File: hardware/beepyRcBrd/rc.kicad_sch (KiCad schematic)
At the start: 16 parts, among them J15 Conn_01x04, J16 Conn_01x03, J17 Conn_01x02, J20 Conn_01x04, Q4 BSS138LT1G, U12 AT7456ELAH_C42388749, X2 H6OEL89CSC-SUGYLC-27M

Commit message: fix: net names
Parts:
- U12: symbol lscs:AT7456ELAH_C42388749 -> beepyRc_symbols:AT7456ELAH_C42388749
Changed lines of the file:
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@@
 	)
 	(symbol
-		(lib_id "lscs:AT7456ELAH_C42388749")
+		(lib_id "beepyRc_symbols:AT7456ELAH_C42388749")
 		(at 68.58 162.56 0)
 		(unit 1)

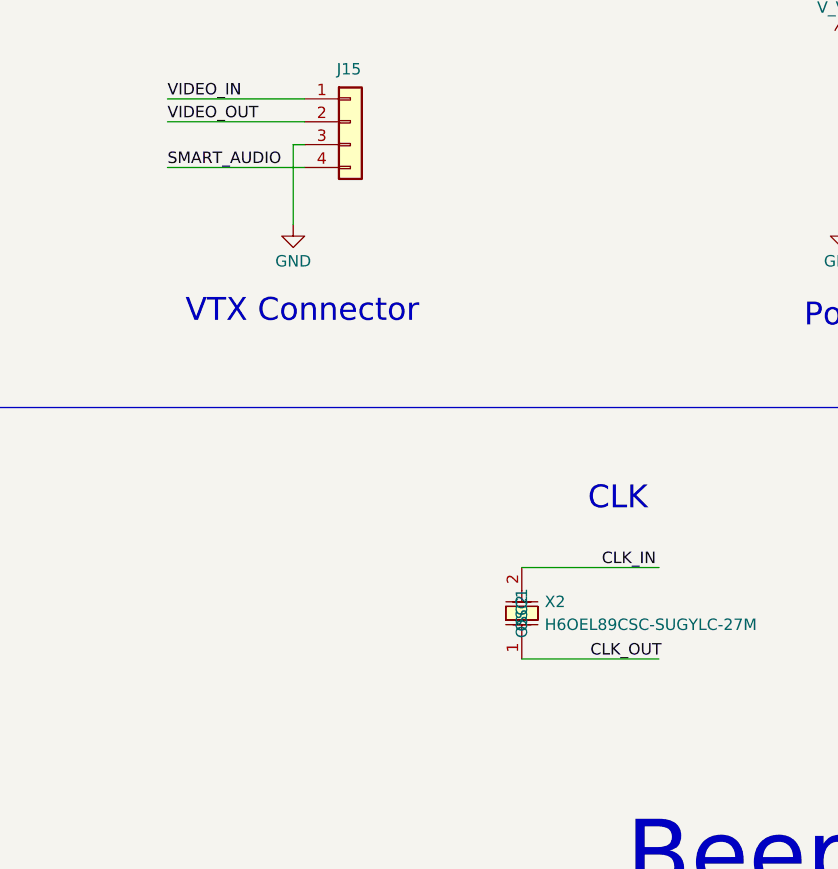
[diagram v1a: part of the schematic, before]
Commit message: fix: passing schematics ERC rules
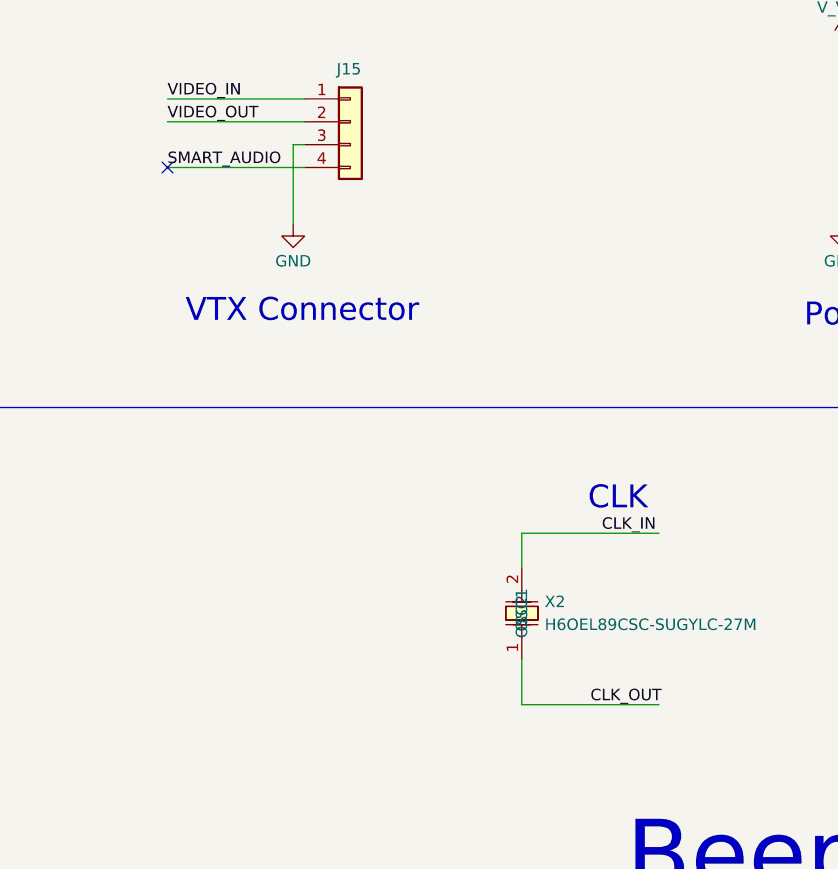
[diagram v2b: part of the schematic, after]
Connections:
- no-connect marks 0 -> 1
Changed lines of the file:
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@@
 		(color 0 0 0 0)
 	)
+	(no_connect
+		(at 158.75 96.52)
+	)
 	(wire
 		(pts
@@
 	(wire
 		(pts
+			(xy 198.12 156.21) (xy 198.12 151.13)
+		)
+		(stroke
+			(width 0)
+			(type default)
+		)
+	)
+	(wire
+		(pts
 			(xy 85.09 152.4) (xy 85.09 167.64)
 		)
@@
 	(wire
 		(pts
+			(xy 198.12 137.16) (xy 198.12 140.97)
+		)
+		(stroke
+			(width 0)
+			(type default)
+		)
+	)
+	(wire
+		(pts
 			(xy 54.61 62.23) (xy 54.61 66.04)
 		)
@@
 	(wire
 		(pts
-			(xy 198.12 151.13) (xy 213.36 151.13)
+			(xy 198.12 156.21) (xy 213.36 156.21)
 		)
 		(stroke
@@
 	(wire
 		(pts
-			(xy 198.12 140.97) (xy 213.36 140.97)
+			(xy 198.12 137.16) (xy 213.36 137.16)
 		)
 		(stroke
@@
 	)
 	(label "CLK_IN"
-		(at 207.01 140.97 0)
+		(at 207.01 137.16 0)
 		(effects
 			(font
@@
 	)
 	(label "CLK_OUT"
-		(at 205.74 151.13 0)
+		(at 205.74 156.21 0)
 		(effects
 			(font

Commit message: feat: completed beepyRcBrd_rev_0_0.pdf
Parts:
- C14, C29, C30, C33, C34, C37: footprint Capacitor_SMD:C_0603_1608Metric_Pad1.08x0.95mm_HandSolder -> beepyRcBrd:C_0603_1608Metric_Pad1.08x0.95mm_HandSolder
- J15, J20: footprint TestPoint:TestPoint_Bridge_Pitch2.54mm_Drill1.0mm -> beepyRcBrd:PinHeader_1x04_P2.54mm_Vertical
- J16: footprint TestPoint:TestPoint_Bridge_Pitch2.54mm_Drill1.0mm -> beepyRcBrd:rc
- J17: footprint TestPoint:TestPoint_Bridge_Pitch2.54mm_Drill1.0mm -> beepyRcBrd:PinHeader_1x02_P2.54mm_Vertical
- Q4: footprint lscs:SOT-23-3_L2.9-W1.6-P1.90-LS2.8-BR -> beepyRcBrd:SOT-23-3_L2.9-W1.6-P1.90-LS2.8-BR
- R20, R33, R34: footprint Resistor_SMD:R_0603_1608Metric_Pad0.98x0.95mm_HandSolder -> beepyRcBrd:R_0603_1608Metric_Pad0.98x0.95mm_HandSolder
- U12: footprint lscs:LGA-16_L6.8-W4.0-P0.65-TL-2EP -> beepyRcBrd:LGA-16_L6.8-W4.0-P0.65-TL-2EP
- X2: footprint lscs:HC-49S_L11.4-W4.8-LS12.7 -> beepyRcBrd:HC-49S_L11.4-W4.8-LS12.7
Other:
- note added: "C33 between AVDD (P12) and AGND (P10) C34 between DVDD (P2) and DGND (P1) C37 between PVDD (P14) and PGND (P11)"
- note removed: "C14 between AVDD (P12) and AGND (P10) C29 between DVDD (P2) and DGND (P1) C30 between PVDD (P14) and PGND (P11)"
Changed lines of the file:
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@@
 		(rev "V0.0")
 		(company "ElectronPlant")
+		(comment 1 "© David Arnaiz 2026")
+		(comment 2 "Licensed under CERN-OHL-S v2")
 	)
 	(text "BeepyRC"
 		(exclude_from_sim no)
-		(at 233.426 173.228 0)
+		(at 252.73 173.99 0)
 		(effects
 			(font
@@
 		)
 	)
-	(text "C14 between AVDD (P12) and AGND (P10)\nC29 between DVDD (P2) and DGND (P1)\nC30 between PVDD (P14) and PGND (P11)"
+	(text "C33 between AVDD (P12) and AGND (P10)\nC34 between DVDD (P2) and DGND (P1)\nC37 between PVDD (P14) and PGND (P11)"
 		(exclude_from_sim no)
 		(at 48.514 47.244 0)
@@
 			)
 		)
-		(property "Footprint" "Capacitor_SMD:C_0603_1608Metric_Pad1.08x0.95mm_HandSolder"
+		(property "Footprint" "beepyRcBrd:C_0603_1608Metric_Pad1.08x0.95mm_HandSolder"
 			(at 101.6 161.5948 0)
 			(effects
@@
 			)
 		)
-		(property "Footprint" "TestPoint:TestPoint_Bridge_Pitch2.54mm_Drill1.0mm"
+		(property "Footprint" "beepyRcBrd:PinHeader_1x04_P2.54mm_Vertical"
 			(at 240.03 44.45 0)
 			(effects
@@
 			)
 		)
-		(property "Footprint" "lscs:SOT-23-3_L2.9-W1.6-P1.90-LS2.8-BR"
+		(property "Footprint" "beepyRcBrd:SOT-23-3_L2.9-W1.6-P1.90-LS2.8-BR"
 			(at 166.37 59.69 0)
 			(effects
@@
 			)
 		)
-		(property "Footprint" "TestPoint:TestPoint_Bridge_Pitch2.54mm_Drill1.0mm"
+		(property "Footprint" "beepyRcBrd:PinHeader_1x02_P2.54mm_Vertical"
 			(at 242.57 91.44 0)
 			(effects
@@
 			)
 		)
-		(property "Footprint" "Capacitor_SMD:C_0603_1608Metric_Pad1.08x0.95mm_HandSolder"
+		(property "Footprint" "beepyRcBrd:C_0603_1608Metric_Pad1.08x0.95mm_HandSolder"
 			(at 101.6 150.1648 0)
 			(effects
@@
 			)
 		)
-		(property "Footprint" "Capacitor_SMD:C_0603_1608Metric_Pad1.08x0.95mm_HandSolder"
+		(property "Footprint" "beepyRcBrd:C_0603_1608Metric_Pad1.08x0.95mm_HandSolder"
 			(at 64.4652 77.47 0)
 			(effects
@@
 			)
 		)
-		(property "Footprint" "Capacitor_SMD:C_0603_1608Metric_Pad1.08x0.95mm_HandSolder"
+		(property "Footprint" "beepyRcBrd:C_0603_1608Metric_Pad1.08x0.95mm_HandSolder"
 			(at 82.2452 77.47 0)
 			(effects
@@
 			)
 		)
-		(property "Footprint" "TestPoint:TestPoint_Bridge_Pitch2.54mm_Drill1.0mm"
+		(property "Footprint" "beepyRcBrd:rc"
 			(at 180.34 49.53 0)
 			(effects
@@
 			)
 		)
-		(property "Footprint" "TestPoint:TestPoint_Bridge_Pitch2.54mm_Drill1.0mm"
+		(property "Footprint" "beepyRcBrd:PinHeader_1x04_P2.54mm_Vertical"
 			(at 179.07 91.44 0)
 			(effects
@@
 			)
 		)
-		(property "Footprint" "Capacitor_SMD:C_0603_1608Metric_Pad1.08x0.95mm_HandSolder"
+		(property "Footprint" "beepyRcBrd:C_0603_1608Metric_Pad1.08x0.95mm_HandSolder"
 			(at 101.6 156.5148 0)
 			(effects
@@
 			)
 		)
-		(property "Footprint" "lscs:HC-49S_L11.4-W4.8-LS12.7"
+		(property "Footprint" "beepyRcBrd:HC-49S_L11.4-W4.8-LS12.7"
 			(at 205.74 146.05 0)
 			(effects
@@
 			)
 		)
-		(property "Footprint" "Capacitor_SMD:C_0603_1608Metric_Pad1.08x0.95mm_HandSolder"
+		(property "Footprint" "beepyRcBrd:C_0603_1608Metric_Pad1.08x0.95mm_HandSolder"
 			(at 73.3552 77.47 0)
 			(effects
@@
 			)
 		)
-		(property "Footprint" "Resistor_SMD:R_0603_1608Metric_Pad0.98x0.95mm_HandSolder"
+		(property "Footprint" "beepyRcBrd:R_0603_1608Metric_Pad0.98x0.95mm_HandSolder"
 			(at 162.052 35.56 90)
 			(effects
@@
 			)
 		)
-		(property "Footprint" "lscs:LGA-16_L6.8-W4.0-P0.65-TL-2EP"
+		(property "Footprint" "beepyRcBrd:LGA-16_L6.8-W4.0-P0.65-TL-2EP"
 			(at 68.58 180.34 0)
 			(effects
@@
 			)
 		)
-		(property "Footprint" "Resistor_SMD:R_0603_1608Metric_Pad0.98x0.95mm_HandSolder"
+		(property "Footprint" "beepyRcBrd:R_0603_1608Metric_Pad0.98x0.95mm_HandSolder"
 			(at 104.902 172.72 90)
 			(effects
@@
 			)
 		)
-		(property "Footprint" "Resistor_SMD:R_0603_1608Metric_Pad0.98x0.95mm_HandSolder"
+		(property "Footprint" "beepyRcBrd:R_0603_1608Metric_Pad0.98x0.95mm_HandSolder"
 			(at 116.84 152.908 90)
 			(effects
